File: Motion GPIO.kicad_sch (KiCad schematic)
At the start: 31 parts, among them J401 Fan PWM, J402 GPIO_CONN, Q401 SIL2301-TP, Q402 EM6K7T2R, U401 BNO085, U402 PCA9575HF, Y401 OM-7604-C7

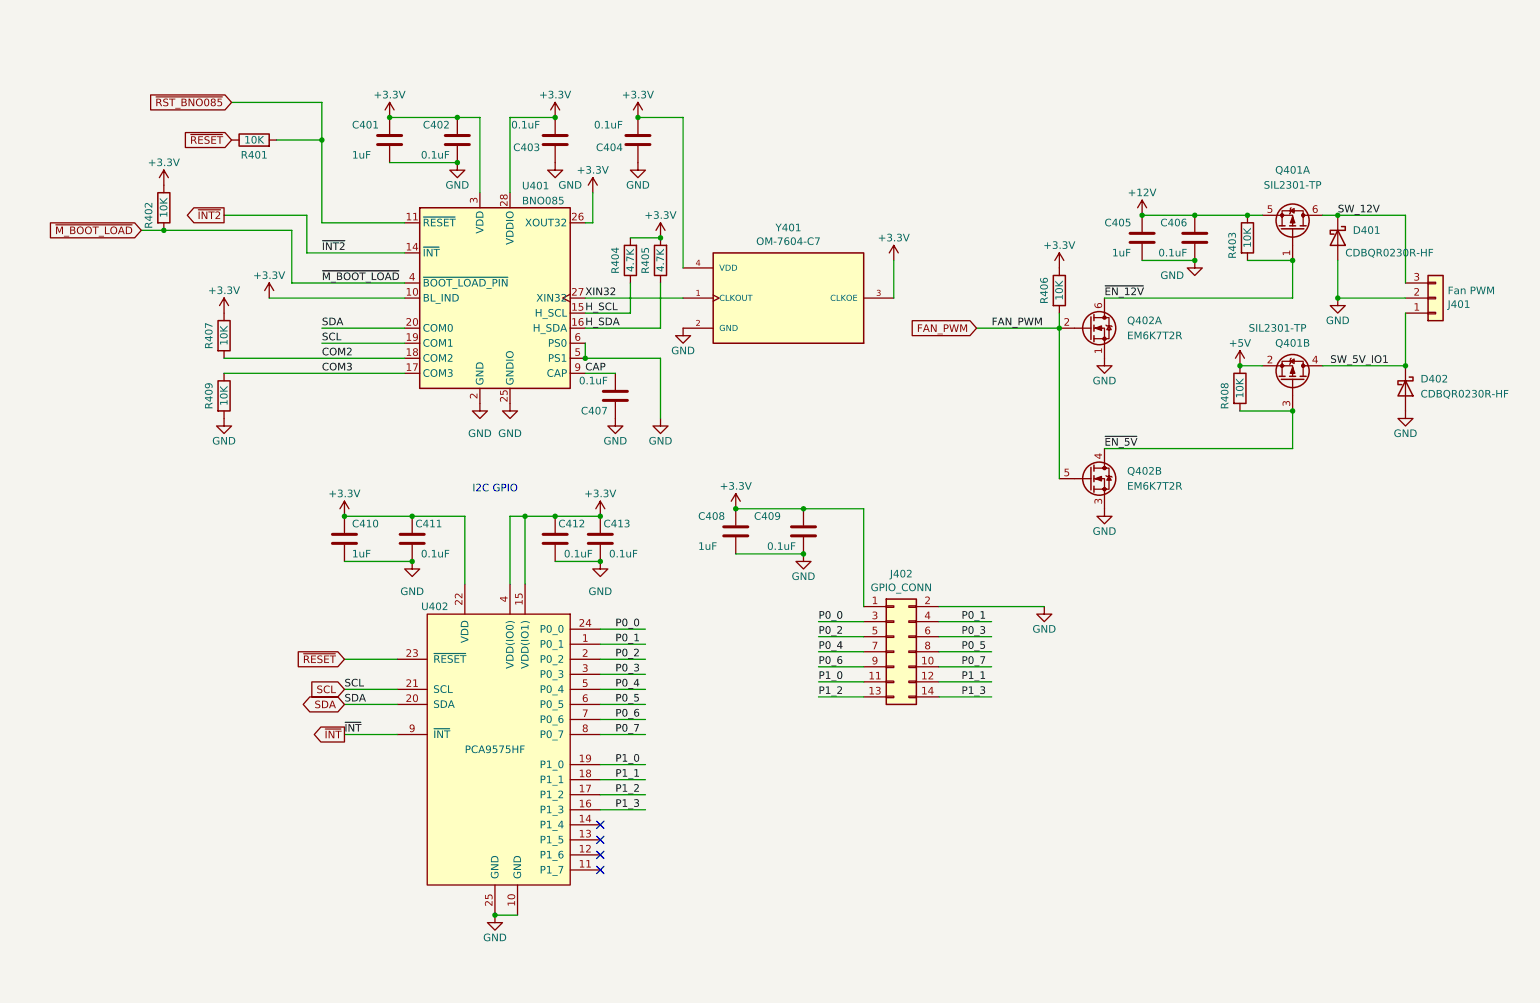
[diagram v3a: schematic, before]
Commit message: Switched to a different 12V booster chip and increased 12V from 500ma to 1A.
Also:
- Switched most 10uF capacitors to 0402 footprints.
- Other cleanup

Signed-off-by: Aaron Williams <aaron.w2@gmail.com>
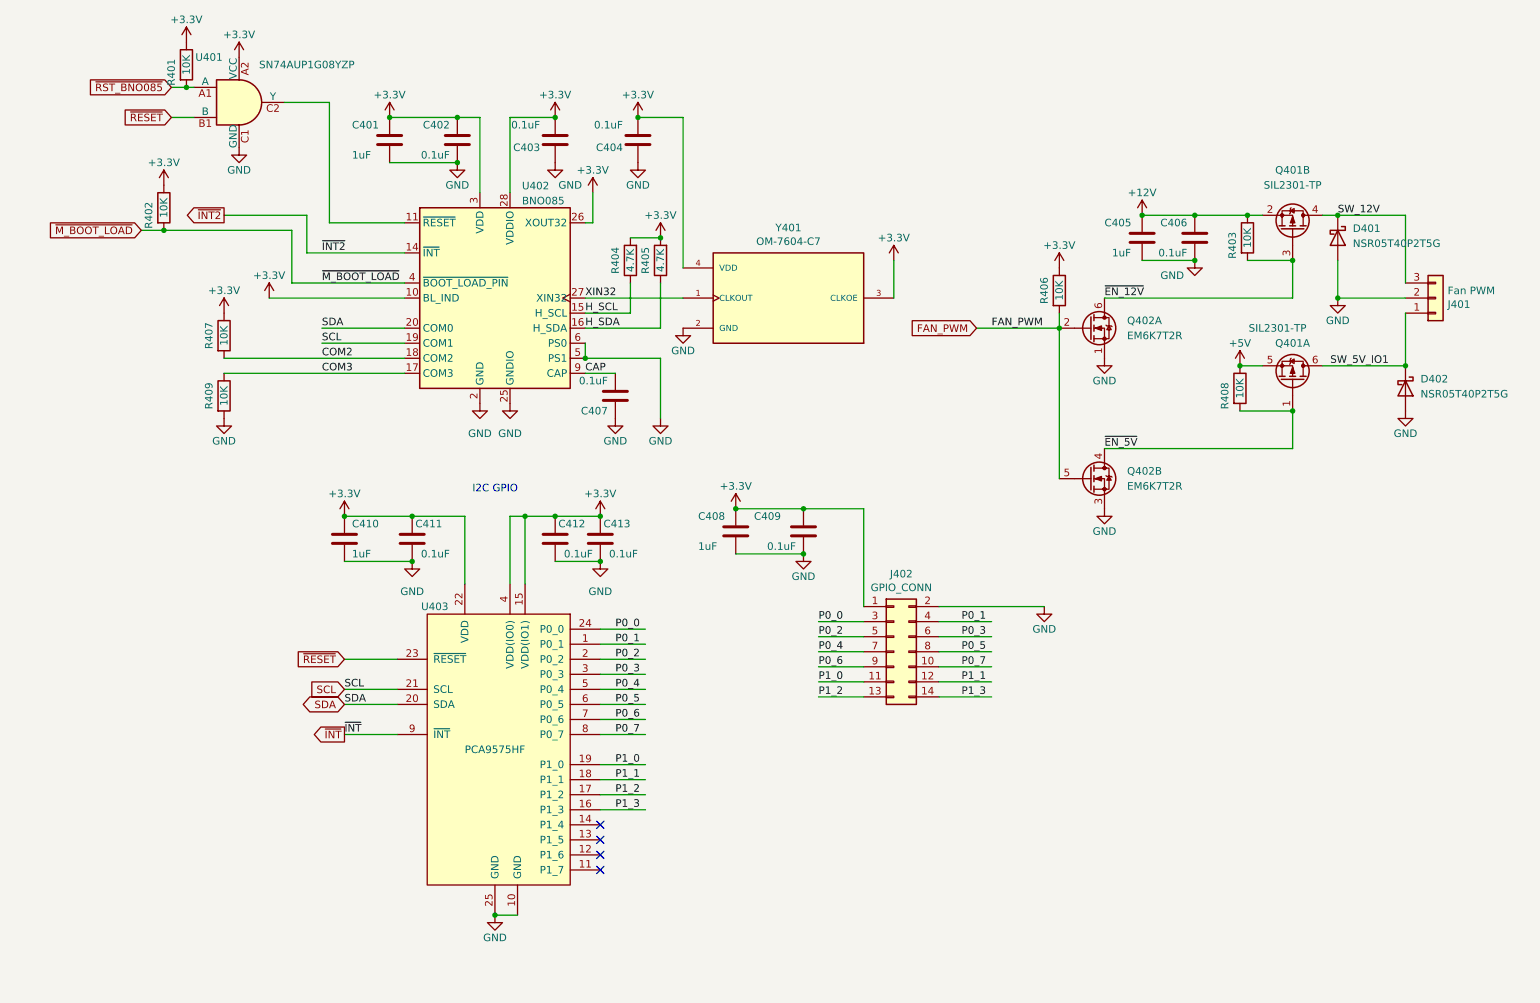
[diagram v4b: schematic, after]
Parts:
- added U401: SN74AUP1G08YZP, Package_BGA:Texas_DSBGA-5_0.9x1.4mm_Layout2x1x2_P0.5mm, symbol 74xx:SN74AUP1G08YZP
- D401, D402: value CDBQR0230R-HF -> NSR05T40P2T5G; footprint Diode_SMD:D_0402_1005Metric -> Diode_SMD:D_SOD-923; MFR Comchip Technology -> onsemi; MPN CDBQR0230R-HF -> NSR05T40P2T5G; SPN 641-2081-1-ND -> (none); SPR Digikey -> (none); SPURL https://www.digikey.com/en/products/detail/comchip-technolo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 -> (none)
- renumbered U401 to U402, U402 to U403
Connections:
- net +12V: now also Q401.2 (S); no longer Q401.5 (S)
- net +3V3: now also R401.1, U401.A2 (VCC)
- net +5V: now also Q401.5 (S); no longer Q401.2 (S)
- net GND: now also U401.C1 (GND)
- net SW_12V: now also Q401.4 (D); no longer Q401.6 (D)
- net SW_5V_IO1: now also Q401.6 (D); no longer Q401.4 (D)
- net ~{EN_12V}: now also Q401.3 (G); no longer Q401.1 (G)
- net ~{EN_5V}: now also Q401.1 (G); no longer Q401.3 (G)
- net ~{RESET}: now also U401.B1 (B); no longer R401.1
- net ~{RST_BNO085}: now also U401.A1 (A); no longer U402.11 (~{RESET})
- new net: U401.C2 (Y), U402.11 (~{RESET})

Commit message: Latest 4.0 settings for pcbway
Signed-off-by: Aaron Williams <aaron.w2@gmail.com>
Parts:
- removed R405: 4.7K, Resistor_SMD:R_0402_1005Metric, symbol Device:R
- removed U403: PCA9575HF, Aaron:HWQFN-24_EP_4x4_Pitch0.5mm, symbol Aaron:PCA9575HF
- added C404, C405: 0.1uF, Capacitor_SMD:C_0402_1005Metric, symbol Device:C
- added C410, C415: 1uF, Capacitor_SMD:C_0402_1005Metric, symbol Device:C
- added R403: 2.2K, Resistor_SMD:R_0402_1005Metric, symbol Device:R
- added U402: BME280, Package_LGA:Bosch_LGA-8_2.5x2.5mm_P0.65mm_ClockwisePinNumbering, symbol Sensor:BME280
- added U404: SX1509BIULTRT, Aaron:QFN-28-1EP_4x4mm_P0.4mm_EP2.65x2.65mm, symbol Aaron:SX1509BIULTRT
- C401: DESC CAP CER 1UF 10V X7R 0603 -> CAP CER 1UF 25V X5R 0402; Digi-Key_PN (none) -> 490-GRM155R61E105MA12JCT-ND; MANUFACTURER (none) -> Murata Electronics; MFR (none) -> Murata Electronics; MPN (none) -> GRM155R61E105MA12J; Manufacturer (none) -> Murata Electronics; Manufacturer Part Number (none) -> GRM155R61E105MA12J; SPN (none) -> 490-GRM155R61E105MA12JCT-ND; SPURL https://www.digikey.com/products/en?keywords=1276-1946-1-ND -> https://www.digikey.com/en/products/detail/murata-electroni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
- C408: renamed from C405; DESC CAP CER 1UF 10V X7R 0603 -> CAP CER 1UF 25V X5R 0402; Digi-Key_PN (none) -> 490-GRM155R61E105MA12JCT-ND; MANUFACTURER (none) -> Murata Electronics; MFR (none) -> Murata Electronics; MPN (none) -> GRM155R61E105MA12J; Manufacturer (none) -> Murata Electronics; Manufacturer Part Number (none) -> GRM155R61E105MA12J; SPN (none) -> 490-GRM155R61E105MA12JCT-ND; SPURL https://www.digikey.com/products/en?keywords=1276-1946-1-ND -> https://www.digikey.com/en/products/detail/murata-electroni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
- C413: renamed from C410; DESC CAP CER 1UF 10V X7R 0603 -> CAP CER 1UF 25V X5R 0402; Digi-Key_PN (none) -> 490-GRM155R61E105MA12JCT-ND; MANUFACTURER (none) -> Murata Electronics; MFR (none) -> Murata Electronics; MPN (none) -> GRM155R61E105MA12J; Manufacturer (none) -> Murata Electronics; Manufacturer Part Number (none) -> GRM155R61E105MA12J; SPN (none) -> 490-GRM155R61E105MA12JCT-ND; SPURL https://www.digikey.com/products/en?keywords=1276-1946-1-ND -> https://www.digikey.com/en/products/detail/murata-electroni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
- C416: renamed from C408; DESC CAP CER 1UF 10V X7R 0603 -> CAP CER 1UF 25V X5R 0402; Digi-Key_PN (none) -> 490-GRM155R61E105MA12JCT-ND; MANUFACTURER (none) -> Murata Electronics; MFR (none) -> Murata Electronics; MPN (none) -> GRM155R61E105MA12J; Manufacturer (none) -> Murata Electronics; Manufacturer Part Number (none) -> GRM155R61E105MA12J; SPN (none) -> 490-GRM155R61E105MA12JCT-ND; SPURL https://www.digikey.com/products/en?keywords=1276-1946-1-ND -> https://www.digikey.com/en/products/detail/murata-electroni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
- D401, D402: SPN (none) -> NSR05T40P2T5GOSCT-ND; SPR (none) -> Digikey; SPURL (none) -> https://www.digikey.com/en/products/detail/onsemi/NSR05T40P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
- J402: MFR (none) -> Adam Tech; MPN (none) -> PH2-14-UA; SPN (none) -> 2057-PH2-14-UA-ND; SPR (none) -> Digikey; SPURL (none) -> https://www.digikey.com/en/products/detail/adam-tech/PH2-14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
- Q401: MFR (none) -> Micro Commercial Co; MPN (none) -> SIL2301-TP; SPN (none) -> SIL2301-TPMSCT-ND; SPR (none) -> Digikey; SPURL (none) -> https://www.digikey.com/en/products/detail/micro-commercial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
- Q402: MFR (none) -> Rohm Semiconductor; MPN (none) -> EM6K7T2R; SPN (none) -> EM6K7T2RCT-ND; SPR (none) -> Digikey; SPURL (none) -> https://www.digikey.com/en/products/detail/rohm-semiconduct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
- R401, R402: DESC (none) -> 10 kOhms ±1% 0.063W, 1/16W Chip Resistor 0402 (1005 Metric)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; Digi-Key_PN (none) -> 311-10.0KLRCT-ND; MANUFACTURER (none) -> YAGEO; MFR (none) -> YAGEO; MPN (none) -> RC0402FR-0710KL; Manufacturer (none) -> YAGEO; Manufacturer Part Number (none) -> RC0402FR-0710KL; SPN 541-2979-1-ND -> 311-10.0KLRCT-ND; SPURL https://www.digikey.com/products/en?keywords=541-2979-1-ND -> https://www.digikey.com/en/products/detail/yageo/RC0402FR-0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; Tolerance 5% -> (none)
- R404: value 4.7K -> 2.2K
- R405: renamed from R407; DESC (none) -> 10 kOhms ±1% 0.063W, 1/16W Chip Resistor 0402 (1005 Metric)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; Digi-Key_PN (none) -> 311-10.0KLRCT-ND; MANUFACTURER (none) -> YAGEO; MFR (none) -> YAGEO; MPN (none) -> RC0402FR-0710KL; Manufacturer (none) -> YAGEO; Manufacturer Part Number (none) -> RC0402FR-0710KL; SPN 541-2979-1-ND -> 311-10.0KLRCT-ND; SPURL https://www.digikey.com/products/en?keywords=541-2979-1-ND -> https://www.digikey.com/en/products/detail/yageo/RC0402FR-0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; Tolerance 5% -> (none)
- R406: renamed from R409; DESC (none) -> 10 kOhms ±1% 0.063W, 1/16W Chip Resistor 0402 (1005 Metric)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; Digi-Key_PN (none) -> 311-10.0KLRCT-ND; MANUFACTURER (none) -> YAGEO; MFR (none) -> YAGEO; MPN (none) -> RC0402FR-0710KL; Manufacturer (none) -> YAGEO; Manufacturer Part Number (none) -> RC0402FR-0710KL; SPN 541-2979-1-ND -> 311-10.0KLRCT-ND; SPURL https://www.digikey.com/products/en?keywords=541-2979-1-ND -> https://www.digikey.com/en/products/detail/yageo/RC0402FR-0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; Tolerance 5% -> (none)
- R407: renamed from R403; value 10K -> 110K; SPN 541-2979-1-ND -> (none); SPR Digikey -> (none); SPURL https://www.digikey.com/products/en?keywords=541-2979-1-ND -> (none); Tolerance 5% -> (none)
- R408: renamed from R406; DESC (none) -> 10 kOhms ±1% 0.063W, 1/16W Chip Resistor 0402 (1005 Metric)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; Digi-Key_PN (none) -> 311-10.0KLRCT-ND; MANUFACTURER (none) -> YAGEO; MFR (none) -> YAGEO; MPN (none) -> RC0402FR-0710KL; Manufacturer (none) -> YAGEO; Manufacturer Part Number (none) -> RC0402FR-0710KL; SPN 541-2979-1-ND -> 311-10.0KLRCT-ND; SPURL https://www.digikey.com/products/en?keywords=541-2979-1-ND -> https://www.digikey.com/en/products/detail/yageo/RC0402FR-0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; Tolerance 5% -> (none)
- R409: renamed from R408; value 10K -> 110K; SPN 541-2979-1-ND -> (none); SPR Digikey -> (none); SPURL https://www.digikey.com/products/en?keywords=541-2979-1-ND -> (none); Tolerance 5% -> (none)
- renumbered C404 to C406, C406 to C409, C412 to C411, C413 to C412, C411 to C414, C409 to C417, U402 to U403
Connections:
- net +3V3: now also C404.1, C405.1, R403.2, U402.2 (CSB), U402.6 (VDDIO), U402.8 (VDD), U404.12 (VDDM), U404.18 (VCC2), U404.4 (VCC1)
- net GND: now also C404.2, C405.2, C410.2, C415.2, U402.1 (GND), U402.5 (SDO), U402.7 (GND), U404.10 (ADDR1), U404.17 (GND), U404.26 (ADDR0), U404.29 (GND), U404.3 (GND)
- net P0_0: now also J402.5 (Pin_5), U404.27 (I/O[0]); no longer J402.3 (Pin_3)
- net P0_1: now also J402.6 (Pin_6), U404.28 (I/O[1]); no longer J402.4 (Pin_4)
- net P0_2: now also J402.3 (Pin_3), U404.1 (I/O[2]); no longer J402.5 (Pin_5)
- net P0_3: now also J402.4 (Pin_4), U404.2 (I/O[3]); no longer J402.6 (Pin_6)
- net P0_4: now also U404.5 (I/O[4])
- net P0_5: now also U404.6 (I/O[5])
- net P0_6: now also U404.7 (I/O[6])
- net P0_7: now also U404.8 (I/O[7])
- net SCL: now also U404.25 (SCL)
- net SDA: now also U404.24 (SDA)
- net SW_12V: now also C410.1
- net ~{INT}: now also U404.9 (~{INT})
- net ~{RESET}: now also U404.23 (~{RESET})
- net ~{BNO085_RST}: now reaches U401.C2 (Y), U403.11 (~{RESET})
- net H_SCL renamed S_SCL
- net S_SCL: now also R403.1, U402.4 (SCK); no longer R404.1
- net H_SDA renamed S_SDA
- net S_SDA: now also R404.1, U402.3 (SDI)
- net P1_0 renamed P0_14
- net P0_14: now also U404.21 (I/O[14])
- net P1_1 renamed P0_15
- net P0_15: now also U404.22 (I/O[15])
- net P1_2 renamed P0_12
- net P0_12: now also U404.19 (I/O[12])
- net P1_3 renamed P0_13
- net P0_13: now also U404.20 (I/O[13])
- net SW_5V_IO1 renamed SW_5V
- net SW_5V: now also C415.1
- new net P0_10: U404.15 (I/O[10])
- new net P0_11: U404.16 (I/O[11])
- new net P0_8: U404.13 (I/O[8])
- new net P0_9: U404.14 (I/O[9])
- no-connect marks 4 -> 1
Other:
- note added: "High for i2c"
- note added: "I2C address 0x3E"
- note added: "I2C address 0x4A"
- note added: "I2C address 0x77"
- note added: "Low for 0x76"
- moved on the sheet: C401, C402, C403, C408, C409, C411, C412, C413, C414, C416, C417, D401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

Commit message: Minor fixes.
Signed-off-by: Aaron Williams <aaron.w2@gmail.com>
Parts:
- added TP401: ~{BNO_RST}, TestPoint:TestPoint_Pad_1.0x1.0mm, symbol Connector:TestPoint
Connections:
- net ~{BNO085_RST}: now also TP401.1
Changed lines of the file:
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@@
   (junction (at 107.95 73.66) (diameter 0) (color 0 0 0 0)
+  )
+  (junction (at 59.69 30.48) (diameter 0) (color 0 0 0 0)
   )
   (junction (at 245.11 129.54) (diameter 0) (color 0 0 0 0)
@@
     (stroke (width 0) (type default) (color 0 0 0 0))
   )
+  (wire (pts (xy 59.69 30.48) (xy 57.15 30.48))
+    (stroke (width 0) (type default) (color 0 0 0 0))
+  )
   (wire (pts (xy 153.67 175.26) (xy 144.78 175.26))
     (stroke (width 0) (type default) (color 0 0 0 0))
@@
     (stroke (width 0) (type default) (color 0 0 0 0))
   )
+  (wire (pts (xy 59.69 30.48) (xy 64.77 30.48))
+    (stroke (width 0) (type default) (color 0 0 0 0))
+  )
   (wire (pts (xy 88.9 134.62) (xy 96.52 134.62))
     (stroke (width 0) (type default) (color 0 0 0 0))
@@
   )
   (wire (pts (xy 200.66 87.63) (xy 209.55 87.63))
-    (stroke (width 0) (type default) (color 0 0 0 0))
-  )
-  (wire (pts (xy 64.77 30.48) (xy 57.15 30.48))
     (stroke (width 0) (type default) (color 0 0 0 0))
   )
@@
     )
     (property "Datasheet" "" (id 3) (at 86.36 36.83 0)
+      (effects (font (size 1.27 1.27)) hide)
+    )
+    (pin "1")
+  )
+  (symbol (lib_id "Connector:TestPoint") (at 59.69 30.48 0) (unit 1)
+    (in_bom no) (on_board yes) (fields_autoplaced)
+    (property "Reference" "TP401" (id 0) (at 62.23 25.9079 0)
+      (effects (font (size 1.27 1.27)) (justify left))
+    )
+    (property "Value" "~{BNO_RST}" (id 1) (at 62.23 29.0829 0)
+      (effects (font (size 1.27 1.27)) (justify left))
+    )
+    (property "Footprint" "TestPoint:TestPoint_Pad_1.0x1.0mm" (id 2) (at 64.77 30.48 0)
+      (effects (font (size 1.27 1.27)) hide)
+    )
+    (property "Datasheet" "~" (id 3) (at 64.77 30.48 0)
       (effects (font (size 1.27 1.27)) hide)
     )
@@
     (in_bom yes) (on_board yes)
     (property "Reference" "U401" (id 0) (at 44.45 22.86 0))
-    (property "Value" "SN74AUP1G08YZP " (id 1) (at 60.96 24.13 0))
+    (property "Value" "SN74AUP1G08YZP " (id 1) (at 60.96 22.86 0))
     (property "Footprint" "Package_BGA:Texas_DSBGA-5_0.9x1.4mm_Layout2x1x2_P0.5mm" (id 2) (at 49.53 30.48 0)
       (effects (font (size 1.27 1.27)) hide)
